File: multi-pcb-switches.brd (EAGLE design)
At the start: 36.5 x 41.9 mm, 8 parts, among them Q1 BS170, X1 6B-ZR

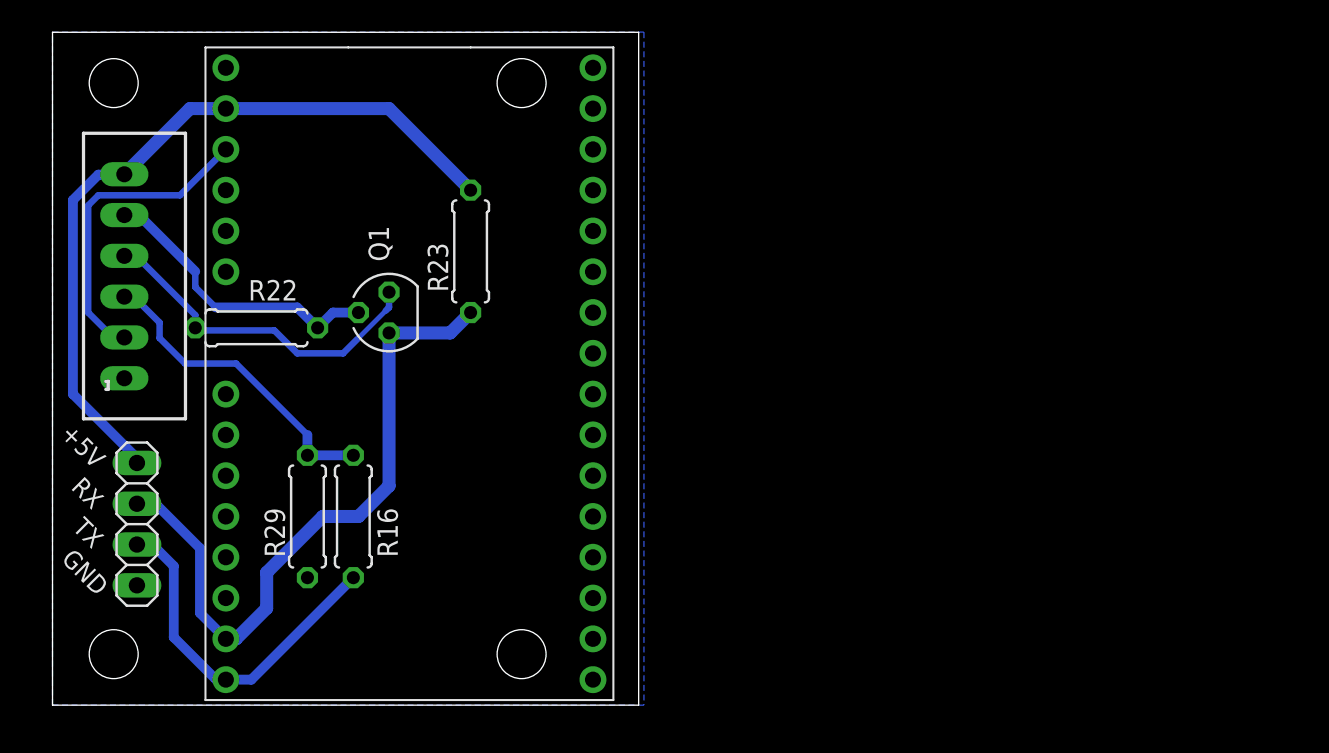
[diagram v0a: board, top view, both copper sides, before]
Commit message: Routed more multi-pcb boards
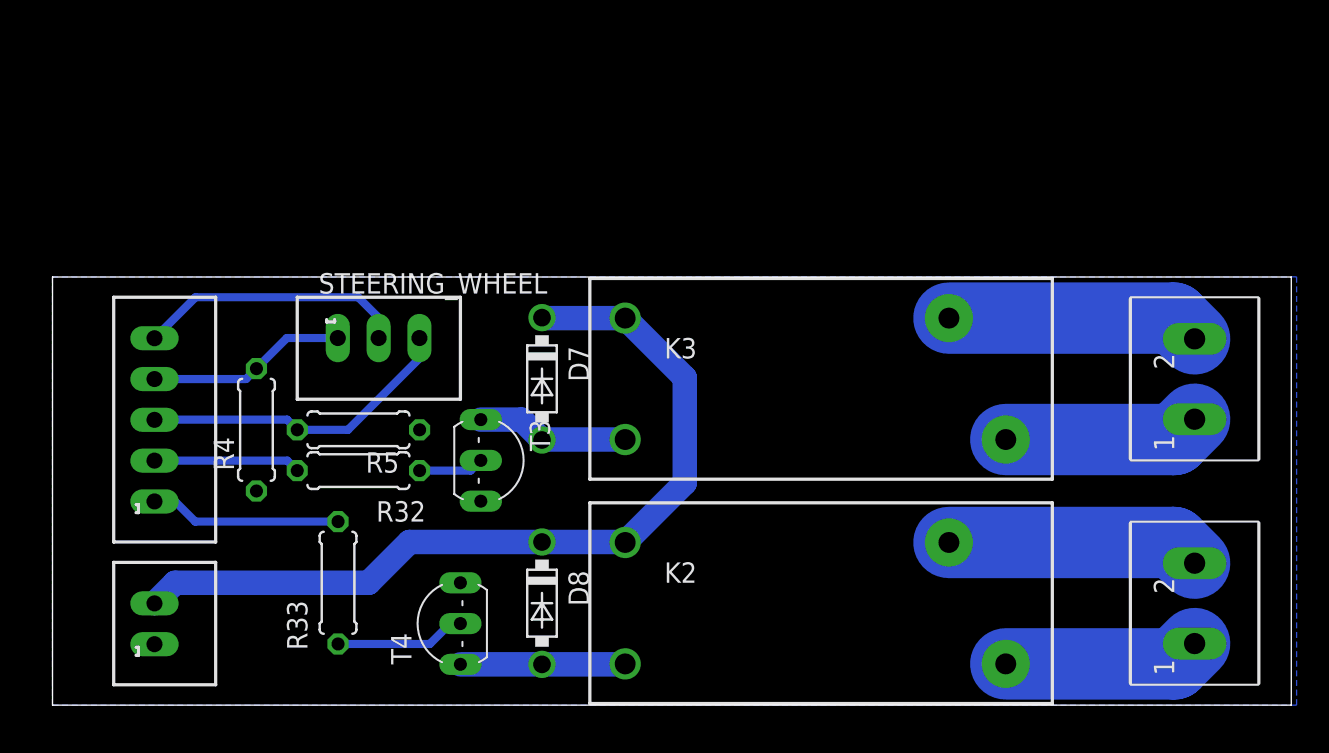
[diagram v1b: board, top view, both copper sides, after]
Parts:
- removed JP_UART2: (no value), pinhead:1X04
- removed Q1: BS170, transistor-small-signal:SOT54E
- removed R16: 5k, rcl:0207/7
- removed R22, R23, R29: 10k, rcl:0207/7
- removed U$6: A9G, A9:A9G
- removed X1: 6B-ZR, con-jst-custom:B6B-ZR2.5
- added CLAXON_CONN, ENGINE_CUTOFF_CONN: (no value), con-ptr500-custom:AK300/2
- added D7, D8: 1N40047, diode-custom:DO41-7.6
- added K2, K3: RT184012, relay:RT-N/O12A3.5
- added R32, R33: 2k, rcl:0207/7
- added R4, R5: 680, rcl:0207/7
- added STEERING_WHEEL: 2.53B-ZR, con-jst-custom:B3B-ZR2.5
- added T3, T4: BC618, transistor-npn:TO92-EBC
- added X3: 2.55B-ZR, con-jst-custom:B5B-ZR2.5
- added X5: 2.52B-ZR, con-jst-custom:B2B-ZR2.5
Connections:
- removed net +5V: JP_UART2.4, R23.2, U$6.5V, X1.6
- removed net GPS_RX: JP_UART2.3, Q1.D, R23.1, U$6.IO0
- removed net GPS_TX: JP_UART2.2, R16.1, U$6.IO1
- removed net MCU_RESET: U$6.RST, X1.2
- removed net UART2_RX: R16.2, R29.2, X1.3
- removed net UART2_TX: Q1.S, R22.1, X1.4
- new net BTN_0: R4.2, STEERING_WHEEL.1, X3.4
- new net BTN_1: R5.2, STEERING_WHEEL.3, X3.3
- new net CLAXON_ENABLE: R33.2, X3.1
- new net ENGINE_CUTOFF_DISABLE: R32.2, X3.2
- new net N$19: ENGINE_CUTOFF_CONN.2, K3.11
- new net N$20: ENGINE_CUTOFF_CONN.1, K3.14
- new net N$22: D7.A, K3.A1, T3.C
- new net N$23: D8.A, K2.A1, T4.C
- new net N$25: R33.1, T4.B
- new net N$26: R32.1, T3.B
- new net N$27: CLAXON_CONN.2, K2.11
- new net N$28: CLAXON_CONN.1, K2.14
- new net PWR_IN+: D7.C, D8.C, K2.A2, K3.A2, X5.2
- net +3V3: now also STEERING_WHEEL.2, X3.5; no longer Q1.G, R22.2, X1.5
- net GND: now also R4.1, R5.1, T3.E, T4.E, X5.1; no longer JP_UART2.1, R29.1, U$6.GND, U$6.GND2, X1.1
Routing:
- net PWR_IN+: track 0.00 -> 53.1 mm
- net +5V: track 47.3 -> 0.00 mm
- net GPS_RX: track 41.9 -> 0.00 mm
- net GPS_TX: track 22.2 -> 0.00 mm
- net UART2_TX: track 21.6 -> 0.00 mm
- net BTN_1: track 0.00 -> 19.9 mm
- net UART2_RX: track 19.7 -> 0.00 mm
- net MCU_RESET: track 19.6 -> 0.00 mm
- net N$27: track 0.00 -> 15.8 mm
- net N$19: track 0.00 -> 15.8 mm
- net BTN_0: track 0.00 -> 12.5 mm
- net N$28: track 0.00 -> 12.3 mm
- net N$20: track 0.00 -> 12.3 mm
- net CLAXON_ENABLE: track 0.00 -> 11.9 mm
- net N$23: track 0.00 -> 10.3 mm
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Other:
- board size 36.5 x 41.9 mm -> 77.1 x 26.7 mm
- board text removed: "+5V"
- board text removed: "GND"
- board text removed: "RX"
- board text removed: "TX"

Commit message: Reduced board spacing
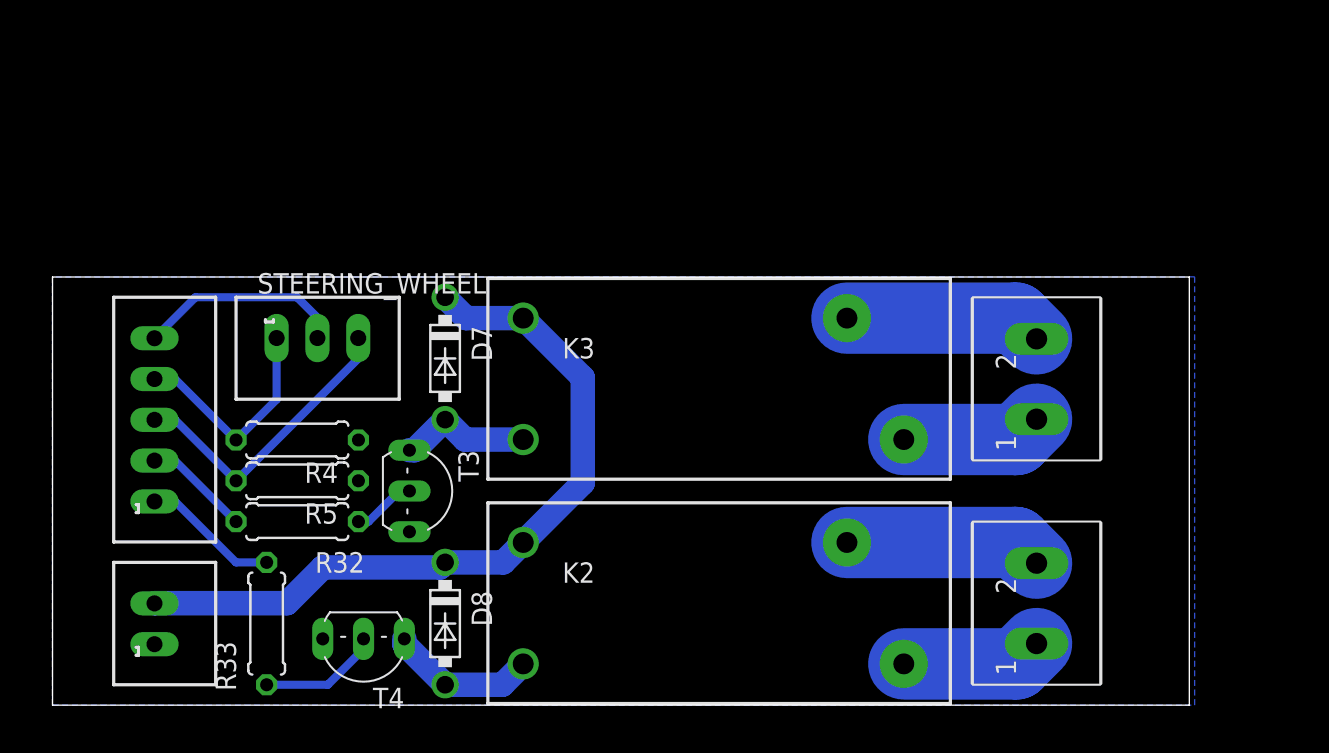
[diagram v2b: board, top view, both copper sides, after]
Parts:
- moved CLAXON_CONN 9.84 mm to (61.3, 6.35)
- moved ENGINE_CUTOFF_CONN 9.84 mm to (61.3, 20.3)
- moved K2 6.35 mm to (41.9, 6.35)
- moved K3 6.35 mm to (41.9, 20.3)
- moved D7 6.16 mm to (24.4, 21.6)
- moved D8 6.16 mm to (24.4, 5.08)
- moved T4 5.26 mm to (19.4, 2.86), turned to 180 degrees
- moved R33 5.12 mm to (13.3, 5.08)
- moved R32 4.96 mm to (15.2, 11.4)
- moved R5 4.96 mm to (15.2, 14.0)
- moved T3 4.84 mm to (23.5, 13.3)
- moved STEERING_WHEEL 3.81 mm to (16.5, 22.9)
- moved R4 2.62 mm to (15.2, 16.5), turned to 180 degrees
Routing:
- net PWR_IN+: track 53.1 -> 47.0 mm
- net +3V3: track 16.8 -> 13.0 mm
- net N$28: track 12.3 -> 8.79 mm
- net N$20: track 12.3 -> 8.79 mm
- net N$27: track 15.8 -> 12.3 mm
- net N$19: track 15.8 -> 12.3 mm
- net CLAXON_ENABLE: track 11.9 -> 8.56 mm
- net ENGINE_CUTOFF_DISABLE: track 9.15 -> 6.65 mm
- net BTN_0: track 12.5 -> 14.0 mm
- net N$22: track 9.53 -> 8.39 mm
- net N$23: track 10.3 -> 9.31 mm
- net N$25: track 8.15 -> 7.59 mm
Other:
- board size 77.1 x 26.7 mm -> 70.8 x 26.7 mm

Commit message: Updated multi-switches board
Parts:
- moved K2 1.91 mm to (43.8, 6.35)
- moved K3 1.91 mm to (43.8, 20.3)
- moved T4 1.91 mm to (21.3, 2.86)
- moved X3 1.91 mm to (8.26, 17.8)
- moved X5 1.91 mm to (8.26, 5.08)
- moved R32 1.90 mm to (17.1, 11.4)
- moved R33 1.90 mm to (15.2, 5.08)
- moved R4 1.90 mm to (17.1, 16.5)
- moved R5 1.90 mm to (17.1, 14.0)
- moved D7 1.90 mm to (26.4, 21.6)
- moved D8 1.90 mm to (26.4, 5.08)
- moved STEERING_WHEEL 1.90 mm to (18.4, 22.9)
- moved T3 1.90 mm to (25.4, 13.3)
- moved CLAXON_CONN 1.90 mm to (63.2, 6.35)
- moved ENGINE_CUTOFF_CONN 1.90 mm to (63.2, 20.3)
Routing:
- net BTN_1: track 20.0 -> 18.7 mm
- net PWR_IN+: track 47.0 -> 46.0 mm
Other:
- board size 70.8 x 26.7 mm -> 72.7 x 27.6 mm
- board text added: "12V"
- board text added: "3V"
- board text added: "BTN0"
- board text added: "BTN1"
- board text added: "GND"
- board text added: "S1"
- board text added: "S2"
